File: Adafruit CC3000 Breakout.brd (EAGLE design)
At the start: 26 x 40 mm, 32 parts, among them U1 CC3000MOD, U3 74HC4050D, X1 2500AT44M0400E

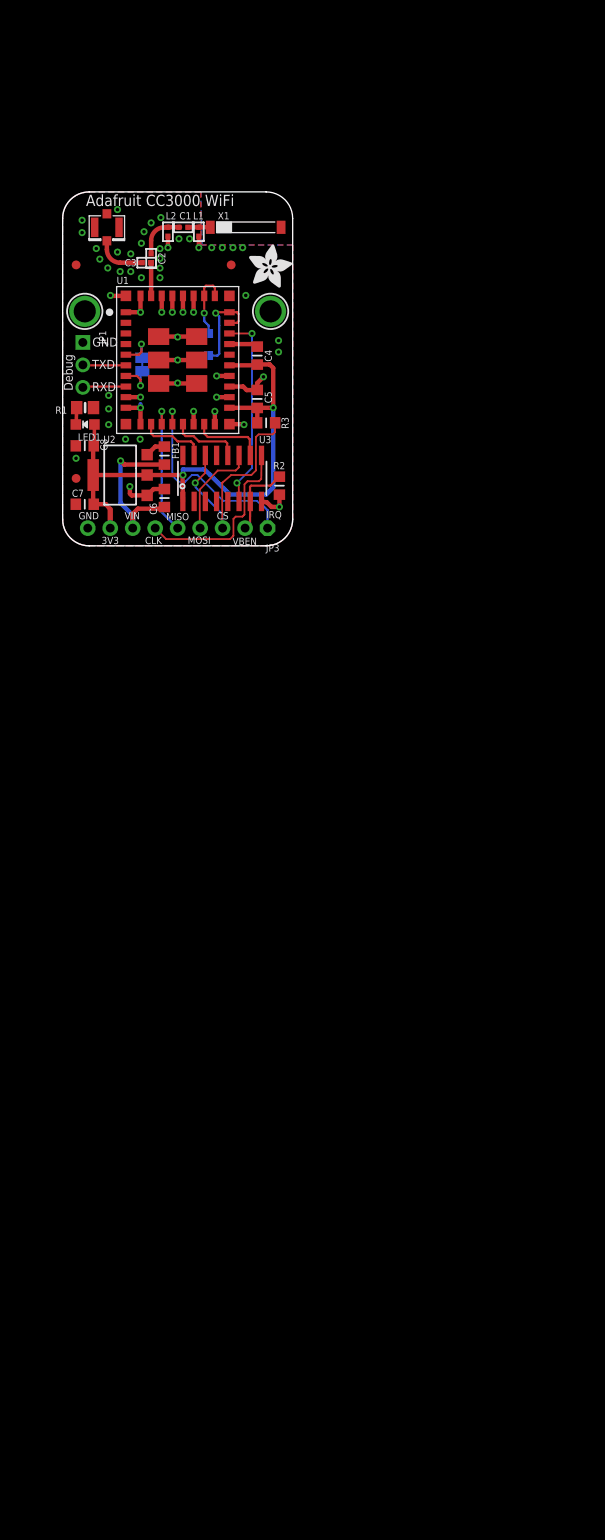
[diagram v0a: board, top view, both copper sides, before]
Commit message: Merge with net widget.
https://github.com/damellis/netwidget
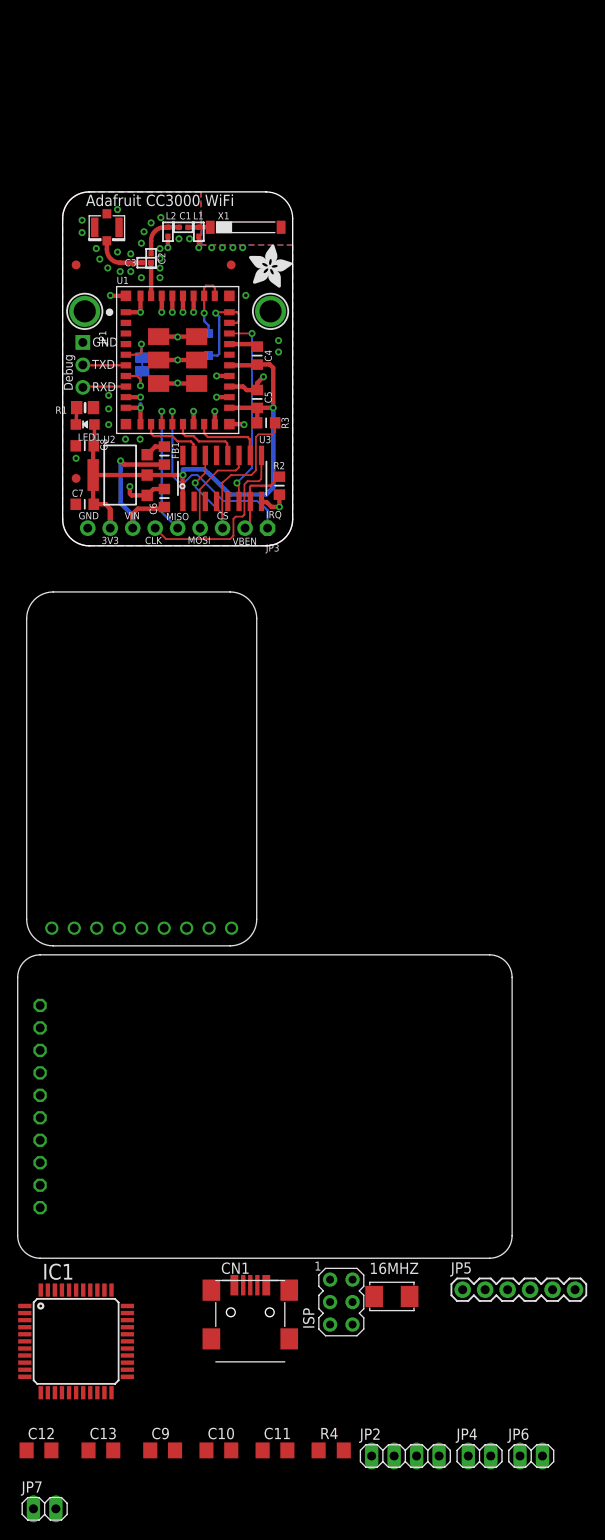
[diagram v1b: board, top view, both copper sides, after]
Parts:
- added 16MHZ: CRYSTAL, Net Widget:2-SMD-5X3MM
- added C10, C9: 18pF, rcl:C1206
- added C11: 10uF, rcl:C1206
- added C12, C13: 0.1uF, rcl:C1206
- added CN1: (no value), Net Widget:USB-MINIB-POWER
- added IC1: ATmega1284P, avr-5:TQFP44
- added ISP: AVRISP-6, adafruit:AVRISP
- added JP2: (no value), pinhead:1X04
- added JP4, JP6, JP7: (no value), pinhead:1X02
- added JP5: FTDI, Net Widget:1X06
- added R4: 10K, rcl:R1206
- added U$39: ADAFRUIT-CC3000-BREAKOUT, Net Widget:ADAFRUIT-CC3000-BREAKOUT
- added U$40: ADAFRUIT-TFT1.8-BREAKOUT, Net Widget:ADAFRUIT-TFT1.8-BREAKOUT
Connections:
- new net 10: IC1.11, JP2.1
- new net 11: IC1.12, JP2.2
- new net 12: IC1.13, JP2.3
- new net 13: IC1.14, JP2.4
- new net 16: IC1.19, JP7.1
- new net 17: IC1.20, JP7.2
- new net 3V3: U$39.P2
- new net A0: IC1.37, JP6.1
- new net A1: IC1.36, JP6.2
- new net AREF: IC1.29
- new net CARD_CS: IC1.21, U$40.P$6
- new net CS: IC1.22, U$39.P7
- new net D/C: IC1.44, U$40.P$7
- new net DTR: C13.2, JP5.DTR
- new net IRQ: IC1.42, U$39.P9
- new net LITE: IC1.43, U$40.P$1
- new net MISO: IC1.2, ISP.1, U$39.P5, U$40.P$2
- new net MOSI: IC1.1, ISP.4, U$39.P6, U$40.P$4
- new net N$10: 16MHZ.P$1, C9.2, IC1.8
- new net N$8: 16MHZ.P$2, C10.2, IC1.7
- new net RESET: C13.1, IC1.4, ISP.5, R4.1
- new net RX: IC1.9, JP5.TXO
- new net SCK: IC1.3, ISP.3, U$39.P4, U$40.P$3
- new net TFT_CS: IC1.40, U$40.P$5
- new net TFT_RESET: IC1.41, U$40.P$8
- new net TX: IC1.10, JP5.RXI
- new net VBEN: IC1.23, U$39.P8
- new net VCC: C11.1, C12.1, CN1.VBUS, IC1.17, IC1.27, IC1.38, IC1.5, ISP.2, JP4.1, JP5.VCC, R4.2, U$39.P3, U$40.P$9
- net GND: now also C10.1, C11.2, C12.2, C9.1, CN1.GND, IC1.18, IC1.28, IC1.39, IC1.6, ISP.6, JP4.2, JP5.GND, U$39.P1, U$40.P$10

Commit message: Smoosh everything together.
Not routed yet, and some passives are 1206 and others are 0805.
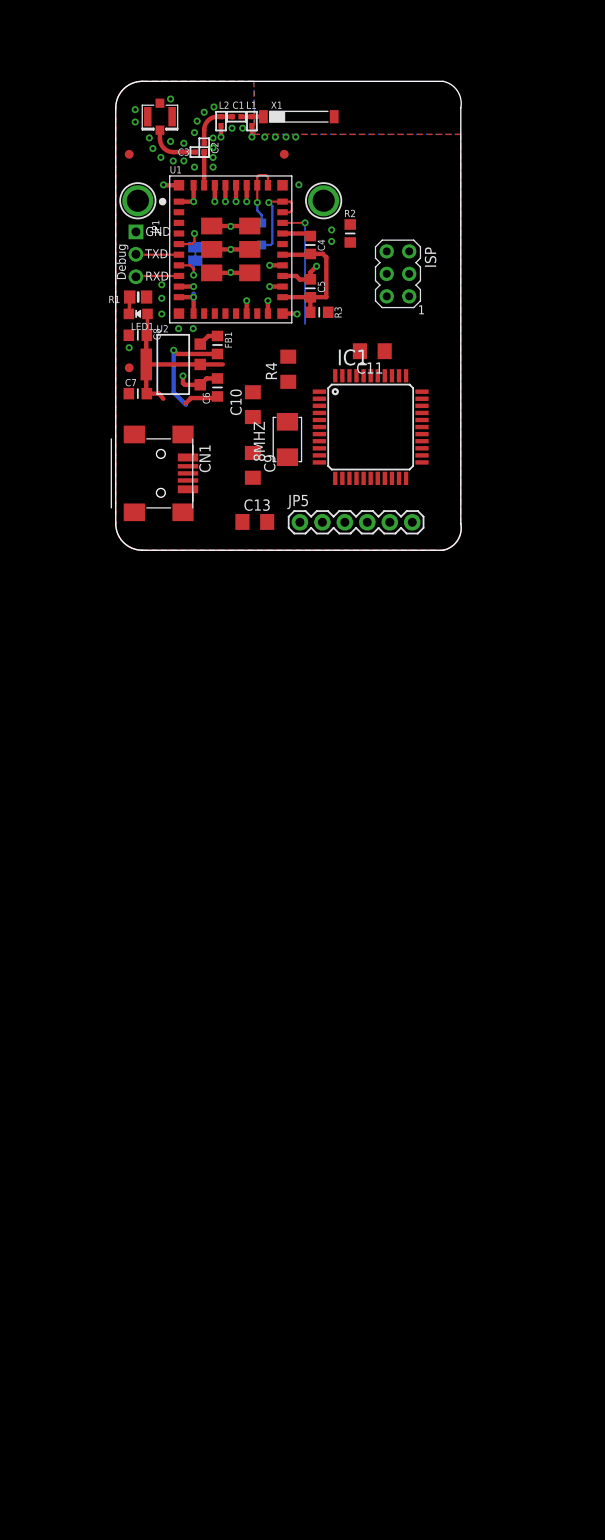
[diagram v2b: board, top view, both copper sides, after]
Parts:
- removed 16MHZ: CRYSTAL, Net Widget:2-SMD-5X3MM
- removed C12: 0.1uF, rcl:C1206
- removed JP2: (no value), pinhead:1X04
- removed JP3: (no value), microbuilder:1X09_ROUND_70
- removed JP4, JP6, JP7: (no value), pinhead:1X02
- removed U$36: (no value), microbuilder:ADAFRUIT_TEXT_20MM
- removed U$39: ADAFRUIT-CC3000-BREAKOUT, Net Widget:ADAFRUIT-CC3000-BREAKOUT
- removed U$40: ADAFRUIT-TFT1.8-BREAKOUT, Net Widget:ADAFRUIT-TFT1.8-BREAKOUT
- removed U$8: (no value), microbuilder:ADAFRUIT_5MM
- removed U3: 74HC4050D, microbuilder:SOIC16
- added 8MHZ: CRYSTAL, Net Widget:2-SMD-5X3MM
- C11: value 10uF -> 0.1uF
- moved C11 124.7 mm to (35.0, 22.0), turned to 180 degrees
- moved R4 122.3 mm to (25.5, 20.0), turned to 90 degrees
- moved C10 118.3 mm to (21.5, 16.0), turned to 90 degrees
- moved ISP 116.4 mm to (37.9, 30.7), turned to 180 degrees
- moved C9 111.8 mm to (21.5, 9.09), turned to 270 degrees
- moved IC1 108.6 mm to (34.8, 13.4)
- moved C13 106.4 mm to (21.7, 2.70)
- moved CN1 97.9 mm to (8.83, 8.19), turned to 270 degrees
- moved JP5 88.7 mm to (26.8, 2.66)
- moved R2 29.6 mm to (32.5, 35.3)
- moved JP1 13.9 mm to (8.29, 32.9)
- moved LED1 13.9 mm to (8.54, 26.2)
- moved C1 13.9 mm to (19.6, 48.5)
- moved C2 13.9 mm to (16.0, 45.0)
- moved C3 13.9 mm to (15.5, 44.5)
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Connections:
- removed net 3V3: U$39.P2
- removed net CARD_CS: IC1.21, U$40.P$6
- removed net CS: IC1.22, U$39.P7
- removed net D/C: IC1.44, U$40.P$7
- removed net IRQ: IC1.42, U$39.P9
- removed net LITE: IC1.43, U$40.P$1
- removed net MISO: IC1.2, ISP.1, U$39.P5, U$40.P$2
- removed net MOSI: IC1.1, ISP.4, U$39.P6, U$40.P$4
- removed net SCK: IC1.3, ISP.3, U$39.P4, U$40.P$3
- removed net SPI_CLK_5V: JP3.6, U3.9
- removed net SPI_CS_5V: JP3.3, R3.2, U3.14
- removed net SPI_MOSI_5V: JP3.4, U3.11
- removed net TFT_CS: IC1.40, U$40.P$5
- removed net TFT_RESET: IC1.41, U$40.P$8
- removed net VBAT_EN_5V: JP3.2, R2.2, U3.7
- removed net VBEN: IC1.23, U$39.P8
- removed net VCC: C11.1, C12.1, CN1.VBUS, IC1.17, IC1.27, IC1.38, IC1.5, ISP.2, JP4.1, JP5.VCC, R4.2, U$39.P3, U$40.P$9
- net 10: no longer JP2.1
- net 11: no longer JP2.2
- net 12: no longer JP2.3
- net 13: no longer JP2.4
- net 16: no longer JP7.1
- net 17: no longer JP7.2
- net A0: no longer JP6.1
- net A1: no longer JP6.2
- net GND: no longer C12.2, JP3.9, JP4.2, U$39.P1, U$40.P$10, U3.8
- net N$10: now also 8MHZ.P$1; no longer 16MHZ.P$1
- net N$8: now also 8MHZ.P$2; no longer 16MHZ.P$2
- net SPI_CLK_3V: now also IC1.3, ISP.3; no longer U3.10
- net SPI_CS_3V: now also IC1.22, R3.2; no longer U3.15
- net SPI_IRQ_3V: now also IC1.42; no longer JP3.1
- net SPI_MISO_3V: now also IC1.2, ISP.1; no longer JP3.5
- net SPI_MOSI_3V: now also IC1.1, ISP.4; no longer U3.12
- net VBAT: now also C11.1, IC1.17, IC1.27, IC1.38, IC1.5, ISP.2, R4.2; no longer JP3.8, U3.1
- net VBAT_EN_3V: now also IC1.23, R2.2; no longer U3.6
- net VIN: now also CN1.VBUS, JP5.VCC; no longer JP3.7
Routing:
- net VBAT: track 64.4 -> 36.5 mm, vias 2 -> 0
- net SPI_CS_5V: track 26.7 -> 0.00 mm, vias 1 -> 0
- net SPI_IRQ_3V: track 23.8 -> 0.00 mm, vias 1 -> 0
- net SPI_CLK_5V: track 21.1 -> 0.00 mm
- net SPI_MISO_3V: track 15.4 -> 0.00 mm, vias 1 -> 0
- net SPI_MOSI_5V: track 11.2 -> 0.00 mm
- net VBAT_EN_5V: track 8.70 -> 0.00 mm
- net SPI_CLK_3V: track 8.62 -> 0.00 mm
- net VBAT_EN_3V: track 22.3 -> 13.9 mm, vias 2 -> 1
- net SPI_MOSI_3V: track 8.08 -> 0.00 mm
- net SPI_CS_3V: track 7.83 -> 0.00 mm
- net GND: track 58.3 -> 54.7 mm, vias 55 -> 54
- net VIN: track 18.8 -> 15.7 mm
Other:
- board size 26 x 40 mm -> 39 x 53 mm
- board text removed: "3V3"
- board text removed: "Adafruit CC3000 WiFi"
- board text removed: "Adafruit CC3000 WiFi 802.11b/g SPI Interface"
- board text removed: "CLK"
- board text removed: "CS"
- board text removed: "IRQ"
- board text removed: "MISO"
- board text removed: "MOSI"
- board text removed: "VBEN"
- board text removed: "VIN"
- board text removed: "Vin: 3-5VDC Logic: 3-5VDC"

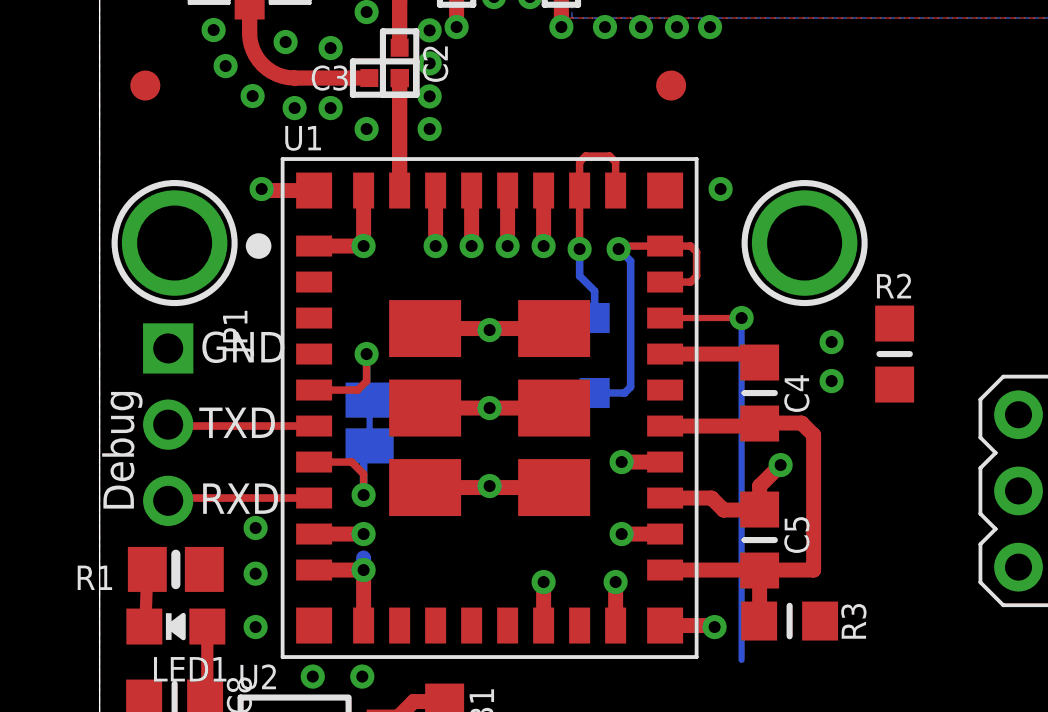
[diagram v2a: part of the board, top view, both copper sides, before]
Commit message: Remove CC3000 RX and TX debug header.
And mounting holes.
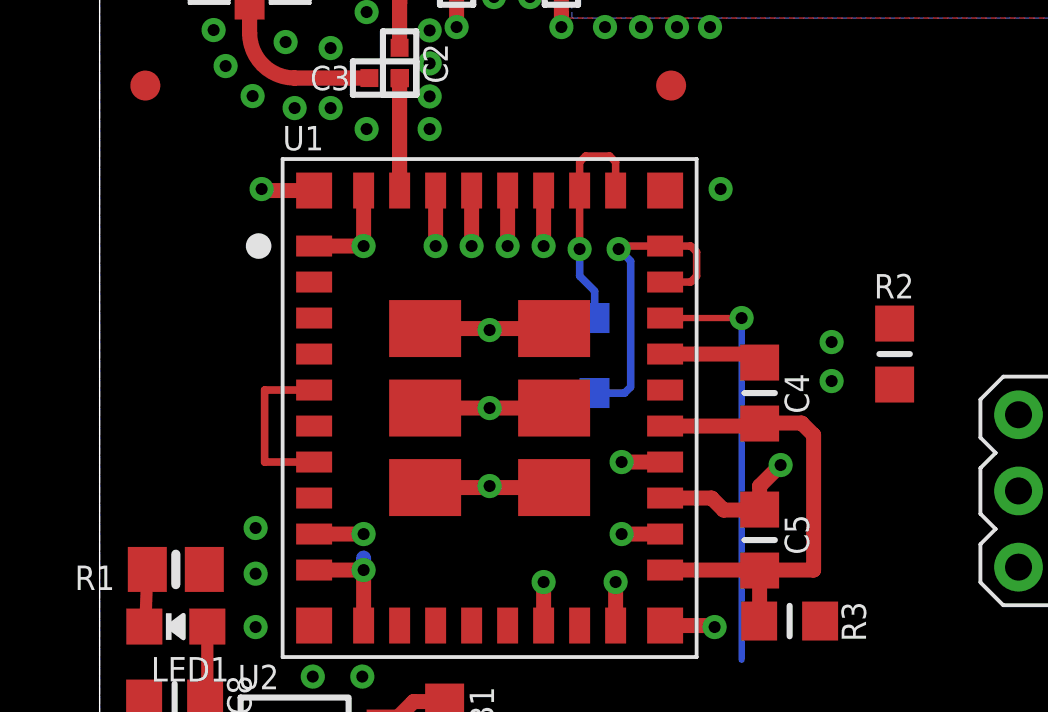
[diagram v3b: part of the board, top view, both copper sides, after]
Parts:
- removed JP1: (no value), microbuilder:1X03_ROUND
- removed SJ1: TESTMODE, microbuilder:SOLDERJUMPER_CLOSEDWIRE
- removed U$24, U$34: MOUNTINGHOLE2.5, microbuilder:MOUNTINGHOLE_2.5_PLATED
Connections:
- removed net N$5: SJ1.2, U1.5
- net GND: no longer JP1.1
- net N$6: now also U1.5; no longer SJ1.1
- net RXD_3V: no longer JP1.3
- net TXD_3V: no longer JP1.2
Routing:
- net RXD_3V: track 4.96 -> 0.00 mm
- net TXD_3V: track 4.91 -> 0.00 mm
- net N$5: track 4.35 -> 0.00 mm, vias 1 -> 0
- net N$6: track 4.24 -> 5.70 mm, vias 1 -> 0
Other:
- board text removed: "Debug"
- board text removed: "GND"
- board text removed: "RXD"
- board text removed: "TXD"
- board text removed: "Test"
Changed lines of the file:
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@@
 <wire x1="9" y1="52.5" x2="6" y2="49.5" width="0" layer="20" curve="90"/>
 <wire x1="6" y1="49.5" x2="6" y2="2.5" width="0" layer="20"/>
-<text x="9.327" y="32.5" size="1.016" layer="21" ratio="16">TXD</text>
-<text x="9.327" y="29.973" size="1.016" layer="21" ratio="16">RXD</text>
-<text x="9.354" y="35.02" size="1.016" layer="21" ratio="16">GND</text>
-<text x="7.143" y="30.026" size="1.016" layer="21" ratio="16" rot="R90">Debug</text>
-<text x="17.303" y="34.471" size="1.016" layer="22" ratio="12" rot="MR270">Test</text>
 </plain>
 <attributes>
@@
 <attribute name="VALUE" x="27.035" y="27.7895" size="1.016" layer="27" font="vector" ratio="10" rot="R90"/>
 </element>
-<element name="SJ1" library="microbuilder" package="SOLDERJUMPER_CLOSEDWIRE" value="TESTMODE" x="15" y="33" smashed="yes" rot="MR90">
-<attribute name="NAME" x="12.87" y="31.949" size="0.8128" layer="26" ratio="18" rot="MR90"/>
-<attribute name="VALUE" x="14.749" y="31.576" size="0.4064" layer="28" ratio="10" rot="MR90"/>
-</element>
 <element name="FID1" library="microbuilder" package="FIDUCIAL_1MM" value="FIDUCIAL&quot;&quot;" x="25.05" y="44.25" smashed="yes">
 <attribute name="BOM" value="EXCLUDE" x="44.1" y="-4.01" size="1.778" layer="27" display="off"/>
@@
 <attribute name="NAME" x="31.5475" y="25.7125" size="0.8128" layer="25" ratio="18" rot="R90"/>
 <attribute name="VALUE" x="30.6875" y="25.129" size="1.016" layer="27" font="vector" ratio="10" rot="R180"/>
-</element>
-<element name="U$24" library="microbuilder" package="MOUNTINGHOLE_2.5_PLATED" value="MOUNTINGHOLE2.5" x="8.5" y="39" smashed="yes">
-<attribute name="BOM" value="EXCLUDE" x="8.5" y="39" size="1.778" layer="27" display="off"/>
-</element>
-<element name="U$34" library="microbuilder" package="MOUNTINGHOLE_2.5_PLATED" value="MOUNTINGHOLE2.5" x="29.5" y="39" smashed="yes">
-<attribute name="BOM" value="EXCLUDE" x="29.5" y="39" size="1.778" layer="27" display="off"/>
 </element>
 <element name="U$35" library="microbuilder" package="U.FL" value="U.FL" x="11" y="48.5" smashed="yes" rot="R270"/>
@@
 <attribute name="NAME" x="6.508" y="28.248" size="0.8128" layer="25" ratio="18" rot="R180"/>
 <attribute name="VALUE" x="4.857" y="28.883" size="1.016" layer="27" font="vector" ratio="10" rot="R180"/>
-</element>
-<element name="JP1" library="microbuilder" package="1X03_ROUND" value="" x="8.286" y="32.947" smashed="yes" rot="R270">
-<attribute name="COMPANY" value="ADAFRUIT INDUSTRIES" x="8.286" y="32.947" size="1.778" layer="27" rot="R270" display="off"/>
-<attribute name="DRAWN" value="KTOWN" x="8.286" y="32.947" size="1.778" layer="27" rot="R270" display="off"/>
-<attribute name="REV" value="C" x="8.286" y="32.947" size="1.778" layer="27" rot="R270" display="off"/>
-<attribute name="NAME" x="10.1148" y="36.8332" size="0.8128" layer="25" ratio="18" rot="R270"/>
-<attribute name="VALUE" x="5.111" y="36.757" size="0.4064" layer="27" ratio="10" rot="R270"/>
 </element>
 <element name="ISP" library="adafruit" package="AVRISP" value="AVRISP-6" x="37.9" y="30.737" rot="R180"/>
@@
 <via x="17" y="43.888" extent="1-16" drill="0.4"/>
 <contactref element="R1" pad="1"/>
-<contactref element="JP1" pad="1"/>
 <via x="7.517" y="22.39" extent="1-16" drill="0.4"/>
 <via x="11.2" y="27.978" extent="1-16" drill="0.4"/>
@@
 <wire x1="24.85" y1="40.75" x2="20.8" y2="40.75" width="0" layer="19" extent="1-1"/>
 <wire x1="26.7" y1="40.8" x2="24.85" y2="40.75" width="0" layer="19" extent="1-1"/>
+<wire x1="36.63" y1="33.277" x2="32.5" y2="34.284" width="0" layer="19" extent="1-1"/>
 <wire x1="7.484" y1="23.8" x2="11.2" y2="26.2" width="0" layer="19" extent="1-1"/>
 <wire x1="7.517" y1="22.39" x2="7.484" y2="23.8" width="0" layer="19" extent="1-1"/>
@@
 <wire x1="21.501" y1="14.557" x2="17.5" y2="18.916" width="0" layer="19" extent="1-1"/>
 <wire x1="21.499" y1="10.493" x2="21.501" y2="14.557" width="0" layer="19" extent="1-1"/>
-<wire x1="8.286" y1="35.487" x2="13.15" y2="38.9" width="0" layer="19" extent="1-1"/>
 <wire x1="29.015" y1="13.422" x2="21.501" y2="14.557" width="0" layer="19" extent="1-1"/>
 <wire x1="34.815" y1="19.222" x2="29.015" y2="13.422" width="0" layer="19" extent="1-1"/>
@@
 <wire x1="40.615" y1="13.422" x2="34.815" y2="19.222" width="0" layer="19" extent="1-1"/>
 <wire x1="35.615" y1="7.622" x2="40.615" y2="13.422" width="0" layer="19" extent="1-1"/>
+<wire x1="39.516" y1="2.66" x2="35.615" y2="7.622" width="0" layer="19" extent="1-1"/>
 <wire x1="14.168" y1="6.387" x2="21.499" y2="10.493" width="0" layer="19" extent="1-1"/>
-<wire x1="39.516" y1="2.66" x2="14.168" y2="6.387" width="0" layer="19" extent="1-1"/>
-<wire x1="36.63" y1="33.277" x2="33.6" y2="22" width="0" layer="19" extent="1-1"/>
 </signal>
 <signal name="N$3">
@@
 <wire x1="38.815" y1="7.622" x2="30.016" y2="26.4" width="0" layer="19" extent="1-1"/>
 </signal>
-<signal name="N$5">
-<contactref element="U1" pad="5"/>
-<contactref element="SJ1" pad="2"/>
-<wire x1="13.15" y1="34.1" x2="14.6" y2="34.1" width="0.25" layer="1"/>
-<wire x1="14.6" y1="34.1" x2="14.9" y2="34.4" width="0.25" layer="1"/>
-<wire x1="14.9" y1="34.4" x2="14.9" y2="35.3" width="0.25" layer="1"/>
-<via x="14.9" y="35.3" extent="1-16" drill="0.4"/>
-<wire x1="14.9" y1="35.3" x2="14.9" y2="33.862" width="0.25" layer="16"/>
-<wire x1="14.9" y1="33.862" x2="15" y2="33.762" width="0.25" layer="16"/>
-</signal>
 <signal name="N$6">
 <contactref element="U1" pad="7"/>
-<contactref element="SJ1" pad="1"/>
-<wire x1="13.15" y1="31.7" x2="14.4" y2="31.7" width="0.25" layer="1"/>
-<wire x1="14.4" y1="31.7" x2="14.8" y2="31.3" width="0.25" layer="1"/>
-<wire x1="14.8" y1="31.3" x2="14.8" y2="30.6" width="0.25" layer="1"/>
-<via x="14.8" y="30.6" extent="1-16" drill="0.4"/>
-<wire x1="14.8" y1="30.6" x2="14.8" y2="32.038" width="0.25" layer="16"/>
-<wire x1="14.8" y1="32.038" x2="15" y2="32.238" width="0.25" layer="16"/>
+<contactref element="U1" pad="5"/>
+<wire x1="13.15" y1="34.1" x2="11.5" y2="34.1" width="0.254" layer="1"/>
+<wire x1="11.5" y1="34.1" x2="11.5" y2="31.7" width="0.254" layer="1"/>
+<wire x1="11.5" y1="31.7" x2="13.15" y2="31.7" width="0.254" layer="1"/>
 </signal>
 <signal name="RXD_3V">
 <contactref element="U1" pad="8"/>
-<contactref element="JP1" pad="3"/>
-<wire x1="13.15" y1="30.5" x2="8.286" y2="30.5" width="0.254" layer="1"/>
-<wire x1="8.286" y1="30.5" x2="8.286" y2="30.407" width="0.254" layer="1"/>
 </signal>
 <signal name="TXD_3V">
 <contactref element="U1" pad="6"/>
-<contactref element="JP1" pad="2"/>
-<wire x1="13.15" y1="32.9" x2="8.286" y2="32.9" width="0.254" layer="1"/>
-<wire x1="8.286" y1="32.9" x2="8.286" y2="32.947" width="0.254" layer="1"/>
 </signal>
 <signal name="VIN">
